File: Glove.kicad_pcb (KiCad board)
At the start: 4 copper layers, 72.8 x 52 mm, 43 parts, among them J1 USB_C_Receptacle_USB2.0, J2 Joystick, Q1 2N7002, Q2 2N7002, U1 LM1117-3.3, U2 ESP32-WROOM-32D, U3 CP2102N-Axx-xQFN24

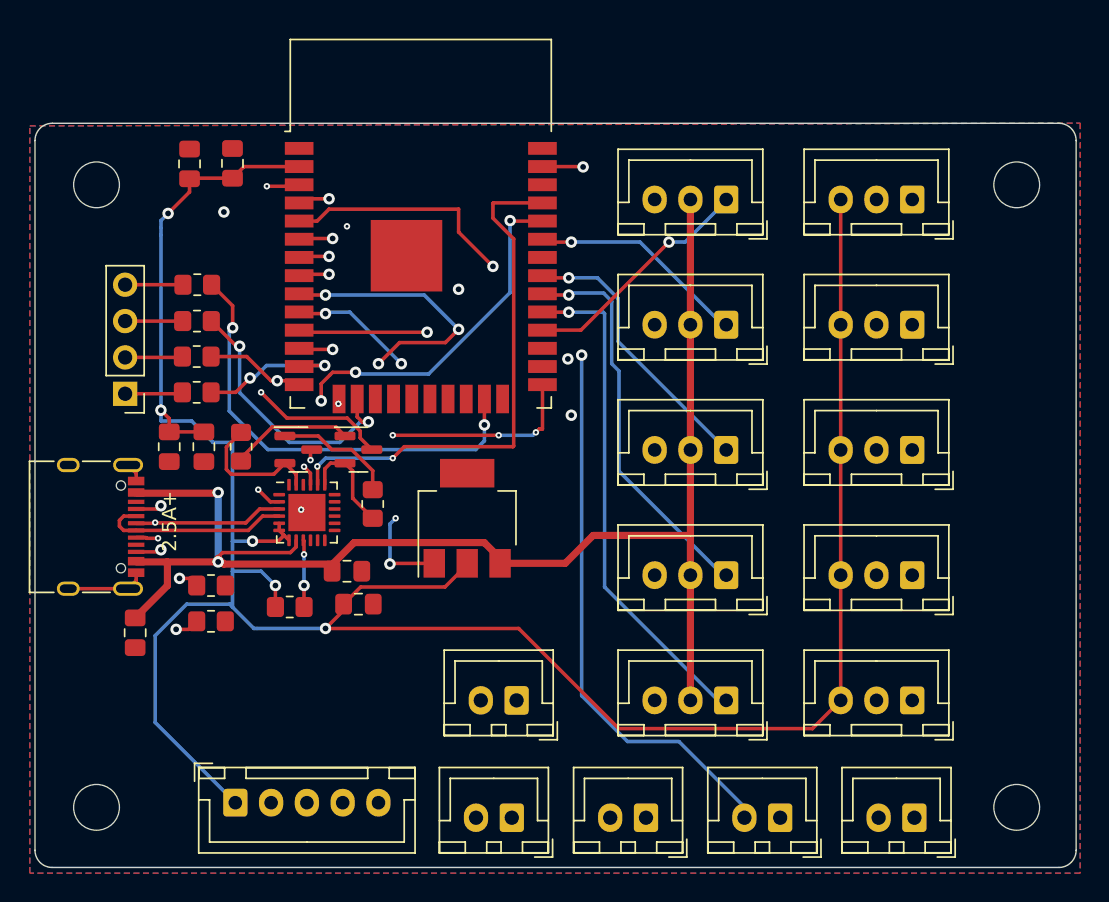
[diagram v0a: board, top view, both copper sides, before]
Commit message: Fix routing, move capacitors closer to ICs
Signed-off-by: Kozova1 <mug66kk@gmail.com>
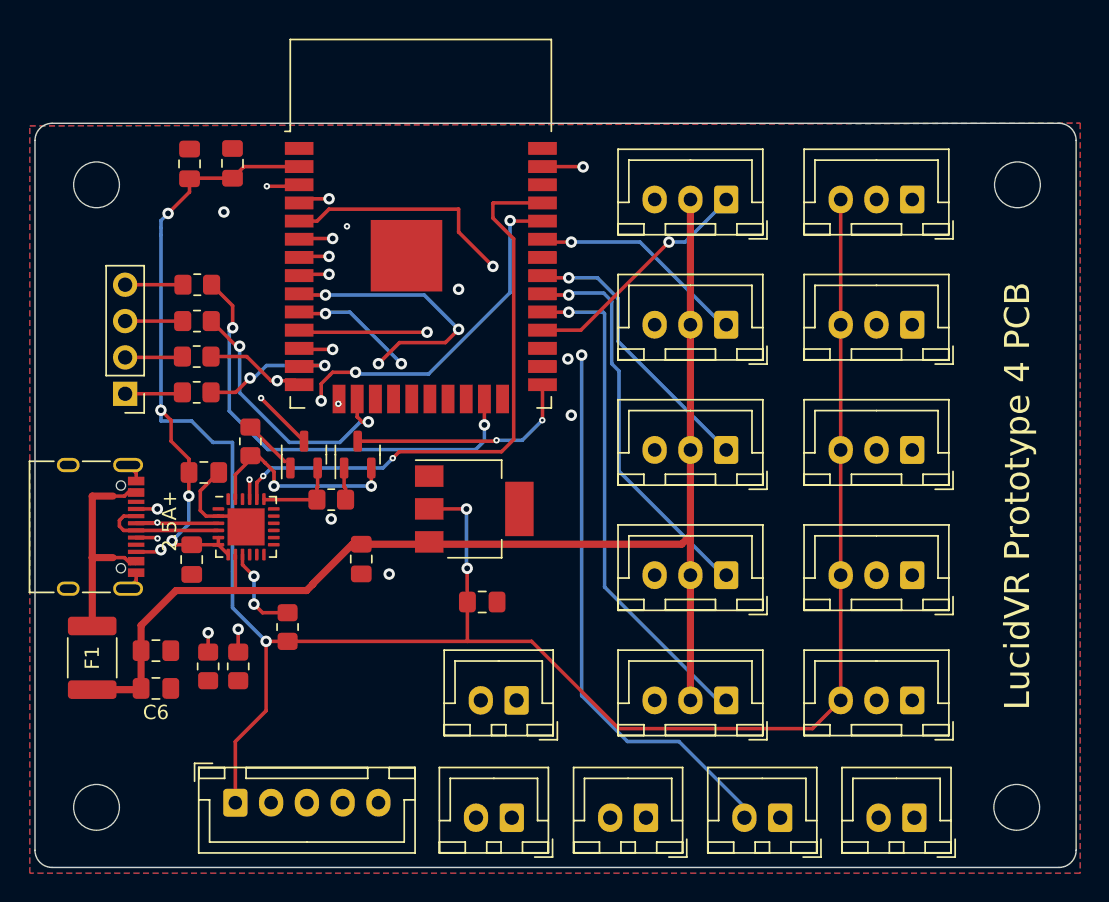
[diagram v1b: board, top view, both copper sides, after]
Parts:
- added C6: 4.7uF, Capacitor_SMD:C_0805_2012Metric_Pad1.18x1.45mm_HandSolder, F.Cu at (118.7, 95.7)
- added F1: 3.5A, Fuse:Fuse_1812_4532Metric_Pad1.30x3.40mm_HandSolder, F.Cu at (114.2, 93.5)
- moved C_Out1 8.65 mm to (141.4, 89.7)
- moved C5 8.04 mm to (121.2, 86.7)
- moved R2 5.96 mm to (124.4, 94.2), turned to -90 degrees
- moved U3 4.37 mm to (125.0, 84.4)
- moved Q2 4.16 mm to (132.8, 79.3), turned to 90 degrees
- moved Q1 3.82 mm to (129.0, 79.3), turned to 90 degrees
- moved R1 3.16 mm to (122.3, 94.2), turned to -90 degrees
- moved R3 2.92 mm to (130.9, 82.5), turned to 0 degrees
- moved C3 1.91 mm to (118.7, 93.0), turned to 180 degrees
- moved C4 1.80 mm to (122.0, 80.6), turned to 0 degrees
- moved R9 1.41 mm to (127.8, 91.4), turned to 90 degrees
- moved C_In1 1.31 mm to (133.0, 86.7), turned to -90 degrees
- moved U1 0.82 mm to (140.9, 83.2), turned to 0 degrees
- moved R8 0.75 mm to (125.2, 78.4), turned to -90 degrees
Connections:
- J1 pad A4: +5V -> Net-(F1-Pad1)
- J1 pad A9: +5V -> Net-(F1-Pad1)
- J1 pad B4: +5V -> Net-(F1-Pad1)
- J1 pad B9: +5V -> Net-(F1-Pad1)
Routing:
- net Net-(F1-Pad1): track 0.00 -> 16.1 mm
- net +5V: track 98.1 -> 86.3 mm, vias 2 -> 0
- net +3V3: track 171.5 -> 164.0 mm, vias 5 -> 7
- net Net-(Q2-Pad1): track 8.46 -> 2.25 mm
- net Net-(J1-PadA5): track 9.84 -> 15.5 mm
- net GND: track 15.2 -> 9.71 mm, vias 7 -> 5
- net Net-(Q2-Pad2): track 9.40 -> 14.7 mm, vias 0 -> 2
- net Net-(Q1-Pad1): track 8.62 -> 3.41 mm
- net IO0: track 21.1 -> 15.9 mm, vias 4 -> 2
- net EN: track 26.5 -> 21.5 mm
- net /D-: track 13.4 -> 8.74 mm
- net RXD: track 36.6 -> 40.9 mm
- net /D+: track 13.5 -> 9.88 mm
- net Net-(R9-Pad2): track 4.68 -> 6.39 mm
- net JoyX: track 56.3 -> 57.9 mm
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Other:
- board text added: "For LucidVR Prototype 4 by Kozova1"
- board text added: "LucidVR Prototype 4 PCB"
- board text removed: "LucidVR PCB for Prototype 4 by Kozova1"

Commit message: Connect all servos and potentiometers in parallel
This saves a bunch of board space.

Signed-off-by: Kozova1 <mug66kk@gmail.com>
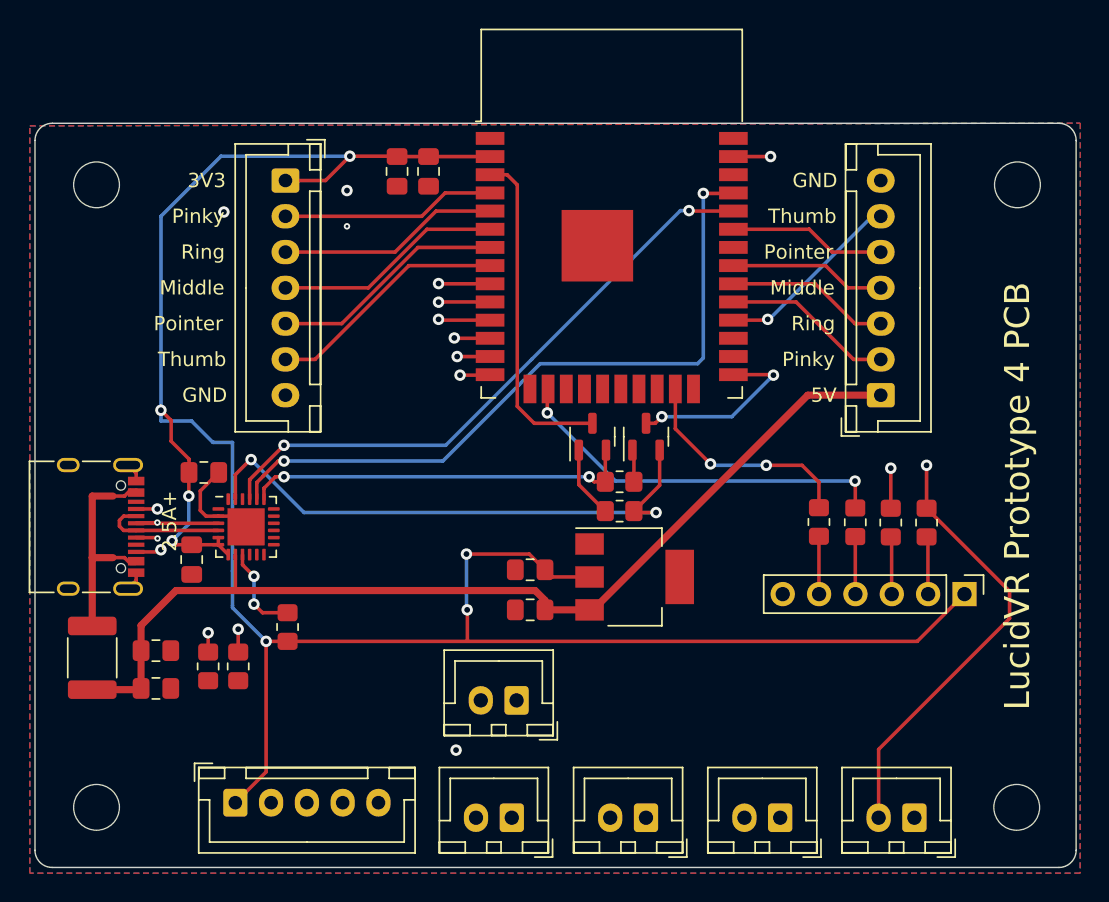
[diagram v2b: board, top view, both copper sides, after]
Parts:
- removed J_JTAG1: Conn_01x04, Connector_PinHeader_2.54mm:PinHeader_1x04_P2.54mm_Vertical
- removed Middle_Servo1: Middle Servo, Connector_JST:JST_XH_B3B-XH-A_1x03_P2.50mm_Vertical
- removed Pinky_Servo1: Pinky Servo, Connector_JST:JST_XH_B3B-XH-A_1x03_P2.50mm_Vertical
- removed Pointer_Servo1: Pointer Servo, Connector_JST:JST_XH_B3B-XH-A_1x03_P2.50mm_Vertical
- removed RV_Middle1: Middle Potentiometer, Connector_JST:JST_XH_B3B-XH-A_1x03_P2.50mm_Vertical
- removed RV_Pinky1: Pinky Potentiometer, Connector_JST:JST_XH_B3B-XH-A_1x03_P2.50mm_Vertical
- removed RV_Pointer1: Pointer Potentiometer, Connector_JST:JST_XH_B3B-XH-A_1x03_P2.50mm_Vertical
- removed RV_Ring1: Ring Potentiometer, Connector_JST:JST_XH_B3B-XH-A_1x03_P2.50mm_Vertical
- removed RV_Thumb1: Thumb Potentiometer, Connector_JST:JST_XH_B3B-XH-A_1x03_P2.50mm_Vertical
- removed Ring_Servo1: Ring Servo, Connector_JST:JST_XH_B3B-XH-A_1x03_P2.50mm_Vertical
- removed Thumb_Servo1: Thumb Servo, Connector_JST:JST_XH_B3B-XH-A_1x03_P2.50mm_Vertical
- added J3: Conn_01x07, Connector_JST:JST_XH_B7B-XH-A_1x07_P2.50mm_Vertical, F.Cu at (169.3, 75.2)
- added J4: Conn_01x07, Connector_JST:JST_XH_B7B-XH-A_1x07_P2.50mm_Vertical, F.Cu at (127.7, 60.2)
- added J5: Conn_01x06, Connector_PinHeader_2.54mm:PinHeader_1x06_P2.54mm_Vertical, F.Cu at (175.2, 89.1)
- moved R4 51.8 mm to (172.5, 84.1), turned to -90 degrees
- moved R5 49.9 mm to (170.0, 84.1), turned to -90 degrees
- moved R6 48.1 mm to (167.5, 84.1), turned to -90 degrees
- moved R7 46.5 mm to (165.0, 84.1), turned to -90 degrees
- moved R8 26.3 mm to (151.1, 83.3), turned to 0 degrees
- moved Q1 20.2 mm to (149.2, 78.1)
- moved Q2 20.2 mm to (152.9, 78.1)
- moved R3 20.2 mm to (151.1, 81.2)
- moved C1 14.5 mm to (135.5, 59.6), turned to -90 degrees
- moved C2 13.7 mm to (137.7, 59.6), turned to -90 degrees
- moved U2 13.4 mm to (150.5, 65.5)
- moved C_In1 12.3 mm to (144.8, 90.2), turned to 180 degrees
- moved U1 12.2 mm to (152.1, 87.9)
- moved C_Out1 4.04 mm to (144.8, 87.4), turned to 180 degrees
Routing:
- net PinkyPot: track 57.4 -> 15.0 mm, vias 3 -> 0
- net MiddlePot: track 54.1 -> 16.0 mm, vias 2 -> 0
- net PointerPot: track 49.6 -> 16.5 mm, vias 1 -> 0
- net RingPot: track 45.0 -> 15.5 mm, vias 1 -> 0
- net ThumbPot: track 44.4 -> 17.0 mm, vias 1 -> 0
- net Net-(Q2-Pad2): track 14.7 -> 39.7 mm
- net PinkyPWM: track 35.5 -> 12.0 mm, vias 1 -> 0
- net BtnTrigger: track 40.6 -> 63.0 mm, vias 1 -> 2
- net Net-(Q1-Pad2): track 5.95 -> 27.3 mm, vias 0 -> 2
- net RingPWM: track 27.8 -> 11.5 mm, vias 1 -> 0
- net +5V: track 86.3 -> 70.2 mm
- net JTAG_MTDO: track 31.7 -> 16.1 mm
- net JoyX: track 57.9 -> 44.8 mm, vias 3 -> 1
- net TXD: track 33.3 -> 43.0 mm, vias 4 -> 2
- net MiddlePWM: track 19.6 -> 10.9 mm, vias 1 -> 0
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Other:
- board text added: "Middle"
- board text added: "Pinky"
- board text added: "Pointer"
- board text added: "Ring"
- board text added: "Thumb"
- board text removed: "For LucidVR Prototype 4 by Kozova1"
- board text removed: "Middle Pot"
- board text removed: "Middle Servo"
- board text removed: "PWM"
- board text removed: "Pinky Pot"
- board text removed: "Pinky Servo"
- board text removed: "Pointer Pot"
- board text removed: "Pointer Servo"
- board text removed: "Ring Pot"
- board text removed: "Ring Servo"
- board text removed: "SIG"
- board text removed: "Thumb Pot"
- board text removed: "Thumb Servo"

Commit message: Add massive changes to routing
Signed-off-by: Kozova1 <mug66kk@gmail.com>
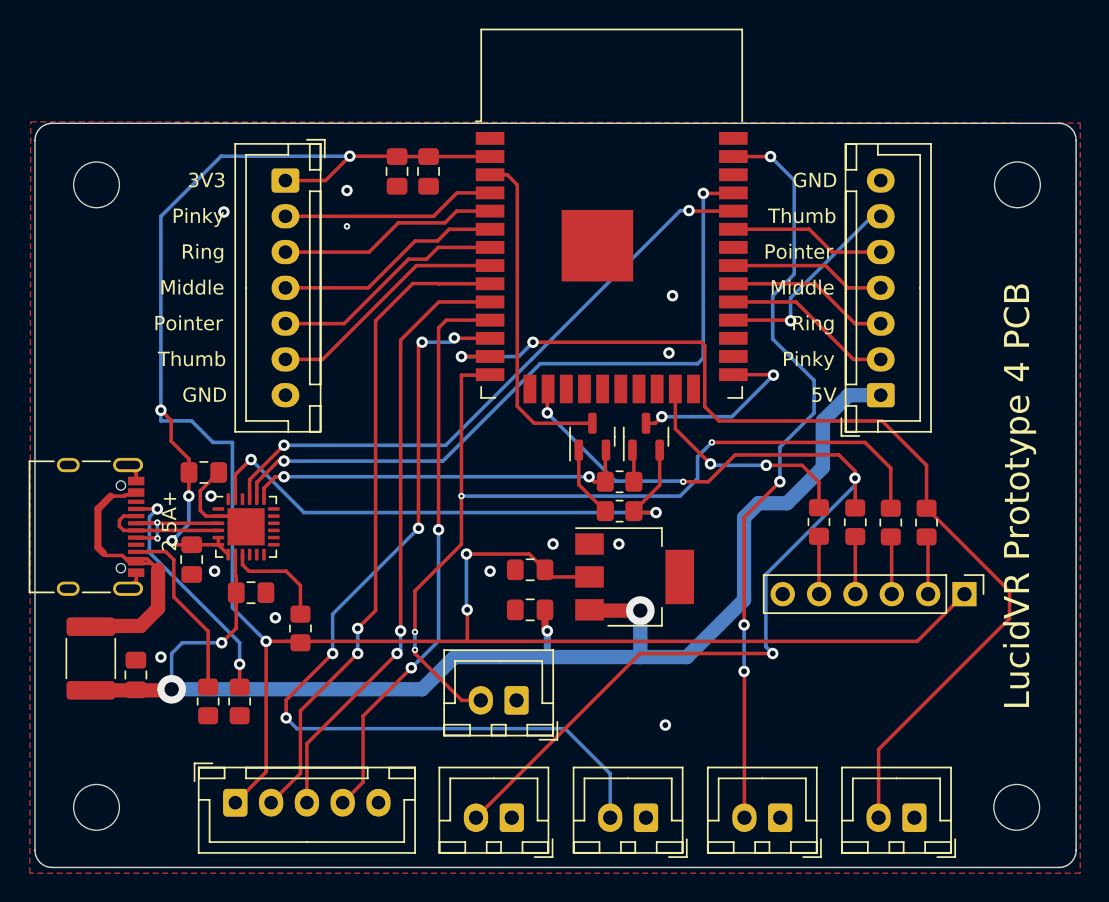
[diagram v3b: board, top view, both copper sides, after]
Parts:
- moved C3 7.79 mm to (125.3, 89.0)
- moved R2 2.45 mm to (124.5, 96.6)
- moved R1 2.45 mm to (122.3, 96.6)
- moved C6 1.69 mm to (117.2, 94.8), turned to -90 degrees
- moved R9 0.91 mm to (128.8, 91.5)
- moved F1 0.11 mm to (114.1, 93.6)
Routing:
- net +5V: track 70.2 -> 92.1 mm, vias 0 -> 4
- net BtnA: track 45.0 -> 62.4 mm, vias 2 -> 5
- net BtnGrab: track 61.3 -> 69.5 mm, vias 2 -> 4
- net Net-(F1-Pad1): track 16.1 -> 20.7 mm
- net Net-(J1-PadB5): track 10.3 -> 12.8 mm, vias 2 -> 0
- net BtnPinch: track 51.0 -> 53.3 mm, vias 1 -> 4
- net BtnB: track 69.5 -> 71.8 mm
- net BtnTrigger: track 63.0 -> 64.8 mm, vias 2 -> 4
- net Net-(J1-PadA5): track 15.5 -> 16.8 mm
- net JoyX: track 44.8 -> 45.8 mm, vias 1 -> 2
- net ThumbPWM: track 13.3 -> 14.3 mm
- net Net-(R9-Pad2): track 6.39 -> 7.36 mm, vias 2 -> 0
- net JoyClick: track 40.2 -> 39.8 mm, vias 1 -> 2
- net JoyY: vias 1 -> 2
- net GND: vias 3 -> 13
- added copper zone on In1.Cu, net GND
- added copper zone on In2.Cu, net GND
- removed copper zone on B.Cu, net GND

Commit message: Sprinkled in some GND vias
Signed-off-by: Kozova1 <mug66kk@gmail.com>
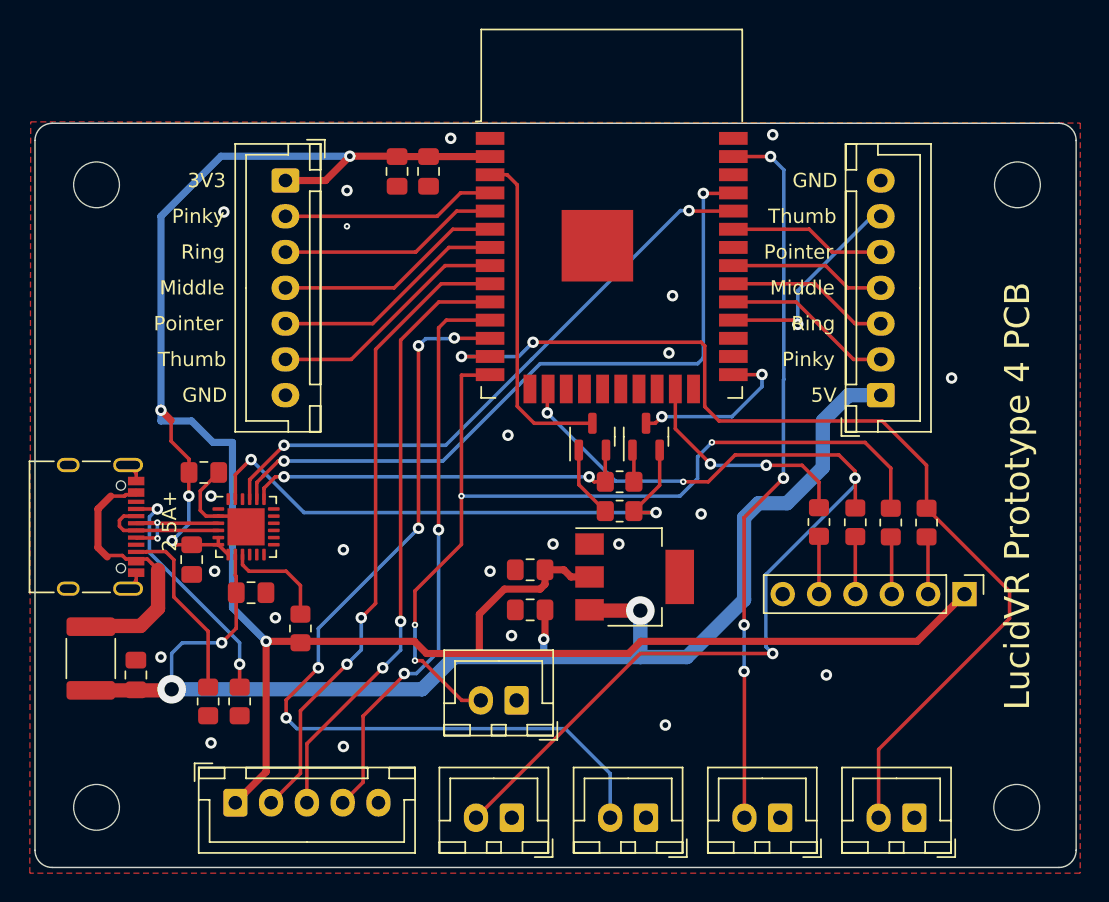
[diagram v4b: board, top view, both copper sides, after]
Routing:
- net BtnPinch: track 53.3 -> 50.3 mm
- net +3V3: track 157.7 -> 155.6 mm, vias 7 -> 5
- net Net-(F1-Pad1): track 20.7 -> 19.2 mm
- net JoyX: track 45.8 -> 44.6 mm
- net IO0: track 13.1 -> 12.0 mm
- net ThumbPWM: track 14.3 -> 14.9 mm
- net GND: vias 13 -> 23

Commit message: Widen 3v3 trace, remove unneeded 2 middle layers
Signed-off-by: Kozova1 <mug66kk@gmail.com>
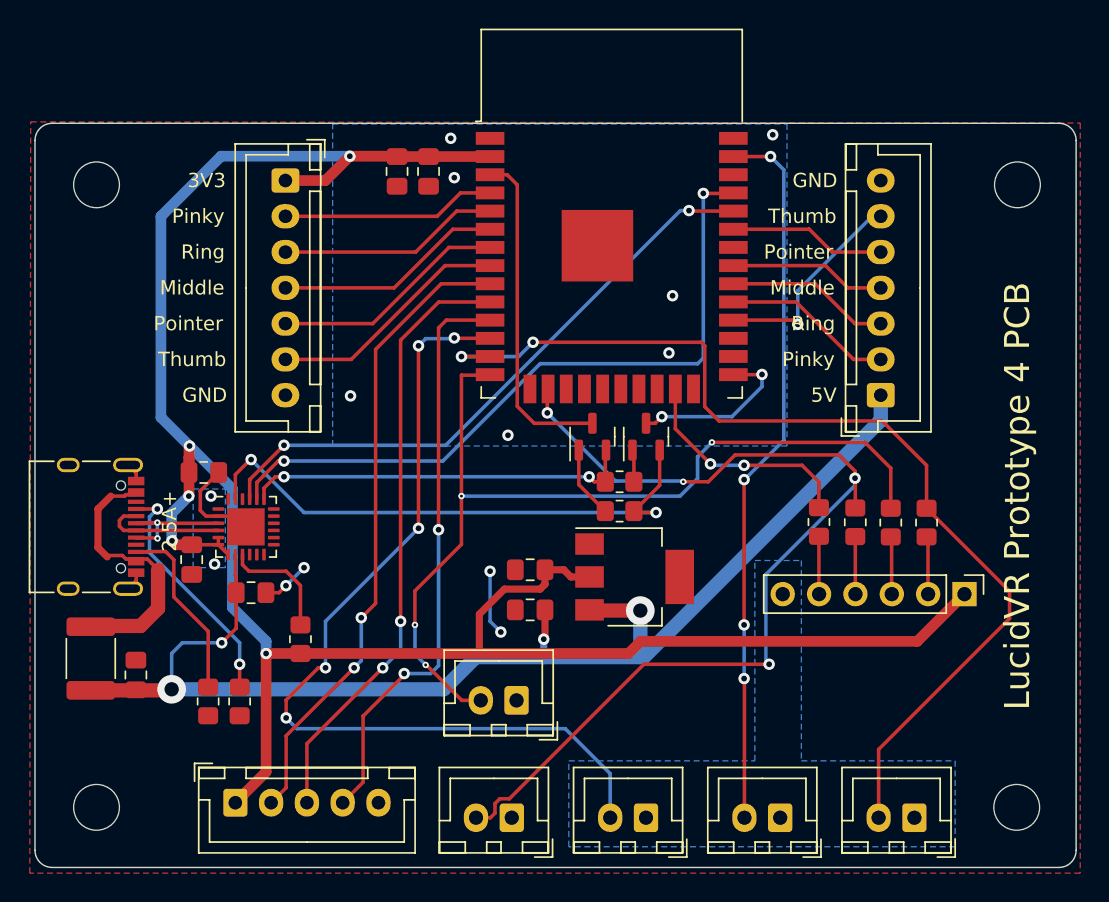
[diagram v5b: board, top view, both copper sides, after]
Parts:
- moved R9 0.75 mm to (128.8, 92.2)
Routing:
- net GND: track 9.57 -> 17.5 mm, vias 23 -> 13
- net +3V3: track 155.6 -> 150.9 mm
- net +5V: track 92.1 -> 87.6 mm
- net Net-(R9-Pad2): track 7.36 -> 8.11 mm
- net JoyClick: track 40.3 -> 40.9 mm
- added copper zone on B.Cu, net GND
- removed copper zone on In1.Cu, net GND
- removed copper zone on In2.Cu, net GND
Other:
- copper layers 4 -> 2
